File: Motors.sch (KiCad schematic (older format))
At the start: 11 parts

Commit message: Eletrical Rules Check
Fixed some label names
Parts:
- gave numbers to parts that had none: 11
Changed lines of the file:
@@
 i_mtr0
 $Comp
-L Connector:Conn_01x12_Female J?
+L Connector:Conn_01x12_Female J4
 U 1 1 5E6AD3E3
 P 8725 2125
-F 0 "J?" H 8753 2101 50  0000 L CNN
+F 0 "J4" H 8753 2101 50  0000 L CNN
 F 1 "Conn_01x12_Female" H 8753 2010 50  0000 L CNN
 F 2 "" H 8725 2125 50  0001 C CNN
@@
 	7975 2725 8525 2725
 $Comp
-L power:GND #PWR?
+L power:GND #PWR055
 U 1 1 5E6B1444
 P 7975 2125
-F 0 "#PWR?" H 7975 1875 50  0001 C CNN
+F 0 "#PWR055" H 7975 1875 50  0001 C CNN
 F 1 "GND" H 7980 1952 50  0000 C CNN
 F 2 "" H 7975 2125 50  0001 C CNN
@@
 $EndComp
 $Comp
-L power:GND #PWR?
+L power:GND #PWR056
 U 1 1 5E6B180E
 P 7975 2725
-F 0 "#PWR?" H 7975 2475 50  0001 C CNN
+F 0 "#PWR056" H 7975 2475 50  0001 C CNN
 F 1 "GND" H 7980 2552 50  0000 C CNN
 F 2 "" H 7975 2725 50  0001 C CNN
@@
 i_mtr1
 $Comp
-L Device:R R?
+L Device:R R20
 U 1 1 5E6FBB13
 P 6425 1250
-F 0 "R?" V 6218 1250 50  0000 C CNN
+F 0 "R20" V 6218 1250 50  0000 C CNN
 F 1 "R" V 6309 1250 50  0000 C CNN
 F 2 "" V 6355 1250 50  0001 C CNN
@@
 enc0_b
 $Comp
-L Device:R R?
+L Device:R R21
 U 1 1 5E700368
 P 6425 1550
-F 0 "R?" V 6218 1550 50  0000 C CNN
+F 0 "R21" V 6218 1550 50  0000 C CNN
 F 1 "R" V 6309 1550 50  0000 C CNN
 F 2 "" V 6355 1550 50  0001 C CNN
@@
 $EndComp
 $Comp
-L Device:R R?
+L Device:R R22
 U 1 1 5E701D8F
 P 6425 1850
-F 0 "R?" V 6218 1850 50  0000 C CNN
+F 0 "R22" V 6218 1850 50  0000 C CNN
 F 1 "R" V 6309 1850 50  0000 C CNN
 F 2 "" V 6355 1850 50  0001 C CNN
@@
 $EndComp
 $Comp
-L Device:R R?
+L Device:R R23
 U 1 1 5E7027C7
 P 6425 2150
-F 0 "R?" V 6218 2150 50  0000 C CNN
+F 0 "R23" V 6218 2150 50  0000 C CNN
 F 1 "R" V 6309 2150 50  0000 C CNN
 F 2 "" V 6355 2150 50  0001 C CNN
@@
 p_enc1
 $Comp
-L Device:Jumper JP?
+L Device:Jumper JP6
 U 1 1 5E67171D
 P 6500 2700
-F 0 "JP?" H 6500 2964 50  0000 C CNN
+F 0 "JP6" H 6500 2964 50  0000 C CNN
 F 1 "Jumper" H 6500 2873 50  0000 C CNN
 F 2 "" H 6500 2700 50  0001 C CNN
@@
 $EndComp
 $Comp
-L Device:Jumper JP?
+L Device:Jumper JP7
 U 1 1 5E673F70
 P 6500 3000
-F 0 "JP?" H 6500 3264 50  0000 C CNN
+F 0 "JP7" H 6500 3264 50  0000 C CNN
 F 1 "Jumper" H 6500 3173 50  0000 C CNN
 F 2 "" H 6500 3000 50  0001 C CNN
@@
 $EndComp
 $Comp
-L Device:Jumper JP?
+L Device:Jumper JP8
 U 1 1 5E6743E1
 P 6500 3300
-F 0 "JP?" H 6500 3564 50  0000 C CNN
+F 0 "JP8" H 6500 3564 50  0000 C CNN
 F 1 "Jumper" H 6500 3473 50  0000 C CNN
 F 2 "" H 6500 3300 50  0001 C CNN
@@
 $EndComp
 $Comp
-L Device:Jumper JP?
+L Device:Jumper JP9
 U 1 1 5E67477A
 P 6500 3600
-F 0 "JP?" H 6500 3864 50  0000 C CNN
+F 0 "JP9" H 6500 3864 50  0000 C CNN
 F 1 "Jumper" H 6500 3773 50  0000 C CNN
 F 2 "" H 6500 3600 50  0001 C CNN
@@
 $EndComp
 $Comp
-L Device:Jumper JP?
+L Device:Jumper JP10
 U 1 1 5E67668F
 P 6500 3900
-F 0 "JP?" H 6500 4164 50  0000 C CNN
+F 0 "JP10" H 6500 4164 50  0000 C CNN
 F 1 "Jumper" H 6500 4073 50  0000 C CNN
 F 2 "" H 6500 3900 50  0001 C CNN
@@
 $EndComp
 $Comp
-L Device:Jumper JP?
+L Device:Jumper JP11
 U 1 1 5E676935
 P 6500 4200
-F 0 "JP?" H 6500 4464 50  0000 C CNN
+F 0 "JP11" H 6500 4464 50  0000 C CNN
 F 1 "Jumper" H 6500 4373 50  0000 C CNN
 F 2 "" H 6500 4200 50  0001 C CNN
@@
 p_enc1
 $Comp
-L ec_2b_rescue:+3.3V #PWR?
+L ec_2b_rescue:+3.3V #PWR052
 U 1 1 5E67786E
 P 5700 2600
-F 0 "#PWR?" H 5700 2450 50  0001 C CNN
+F 0 "#PWR052" H 5700 2450 50  0001 C CNN
 F 1 "+3.3V" H 5715 2773 50  0000 C CNN
 F 2 "" H 5700 2600 50  0001 C CNN
@@
 $EndComp
 $Comp
-L ec_2b_rescue:+12V #PWR?
+L ec_2b_rescue:+12V #PWR054
 U 1 1 5E677F8F
 P 6100 2600
-F 0 "#PWR?" H 6100 2450 50  0001 C CNN
+F 0 "#PWR054" H 6100 2450 50  0001 C CNN
 F 1 "+12V" H 6115 2773 50  0000 C CNN
 F 2 "" H 6100 2600 50  0001 C CNN
@@
 $EndComp
 $Comp
-L ec_2b_rescue:+5V #PWR?
+L ec_2b_rescue:+5V #PWR053
 U 1 1 5E6785E6
 P 5900 2600
-F 0 "#PWR?" H 5900 2450 50  0001 C CNN
+F 0 "#PWR053" H 5900 2450 50  0001 C CNN
 F 1 "+5V" H 5915 2773 50  0000 C CNN
 F 2 "" H 5900 2600 50  0001 C CNN

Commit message: Formatting Changes
Made some minor formatting changes. Documented motor channels. Fixed in labels of motor channel.
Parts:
- removed J4: Conn_01x12_Female, symbol Connector:Conn_01x12_Female
- added J8, J9: Conn_01x06_Female, symbol Connector:Conn_01x06_Female
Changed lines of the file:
@@
 $Descr A4 11693 8268
 encoding utf-8
-Sheet 9 12
+Sheet 6 12
 Title ""
 Date ""
@@
 Text GLabel 3550 1900 0    50   Input ~ 0
 i_mtr0
-$Comp
-L Connector:Conn_01x12_Female J4
-U 1 1 5E6AD3E3
-P 8725 2125
-F 0 "J4" H 8753 2101 50  0000 L CNN
-F 1 "Conn_01x12_Female" H 8753 2010 50  0000 L CNN
-F 2 "" H 8725 2125 50  0001 C CNN
-F 3 "~" H 8725 2125 50  0001 C CNN
-	1    8725 2125
-	1    0    0    -1
-$EndComp
-Text Label 8525 1625 2    50   ~ 0
+Text Label 9525 1625 2    50   ~ 0
 mtr0_out1
-Text Label 8525 1725 2    50   ~ 0
+Text Label 9525 1725 2    50   ~ 0
 mtr0_out2
 Text GLabel 6575 1550 2    50   Input ~ 0
 enc0_a
-Text Label 8525 2225 2    50   ~ 0
+Text Label 9525 2325 2    50   ~ 0
 mtr1_out1
-Text Label 8525 2325 2    50   ~ 0
+Text Label 9525 2425 2    50   ~ 0
 mtr1_out2
 Text GLabel 6575 2150 2    50   Input ~ 0
@@
 enc1_b
 Wire Wire Line
-	7975 2025 8525 2025
-Wire Wire Line
-	7975 2125 8525 2125
-Wire Wire Line
-	7975 2625 8525 2625
-Wire Wire Line
-	7975 2725 8525 2725
+	8975 2025 9525 2025
+Wire Wire Line
+	8975 2125 9525 2125
+Wire Wire Line
+	8975 2725 9525 2725
+Wire Wire Line
+	8975 2825 9525 2825
 $Comp
 L power:GND #PWR055
 U 1 1 5E6B1444
-P 7975 2125
-F 0 "#PWR055" H 7975 1875 50  0001 C CNN
-F 1 "GND" H 7980 1952 50  0000 C CNN
-F 2 "" H 7975 2125 50  0001 C CNN
-F 3 "" H 7975 2125 50  0001 C CNN
-	1    7975 2125
+P 8975 2125
+F 0 "#PWR055" H 8975 1875 50  0001 C CNN
+F 1 "GND" H 8980 1952 50  0000 C CNN
+F 2 "" H 8975 2125 50  0001 C CNN
+F 3 "" H 8975 2125 50  0001 C CNN
+	1    8975 2125
 	1    0    0    -1
 $EndComp
@@
 L power:GND #PWR056
 U 1 1 5E6B180E
-P 7975 2725
-F 0 "#PWR056" H 7975 2475 50  0001 C CNN
-F 1 "GND" H 7980 2552 50  0000 C CNN
-F 2 "" H 7975 2725 50  0001 C CNN
-F 3 "" H 7975 2725 50  0001 C CNN
-	1    7975 2725
-	1    0    0    -1
-$EndComp
-Text Label 8025 2725 0    50   ~ 0
+P 8975 2825
+F 0 "#PWR056" H 8975 2575 50  0001 C CNN
+F 1 "GND" H 8980 2652 50  0000 C CNN
+F 2 "" H 8975 2825 50  0001 C CNN
+F 3 "" H 8975 2825 50  0001 C CNN
+	1    8975 2825
+	1    0    0    -1
+$EndComp
+Text Label 9025 2825 0    50   ~ 0
 mtr_encoder
-Text Label 8025 2125 0    50   ~ 0
+Text Label 9025 2125 0    50   ~ 0
 mtr_encoder
 Text GLabel 6575 1250 2    50   Input ~ 0
@@
 Text GLabel 3550 2800 0    50   Input ~ 0
 i_mtr1
-$Comp
-L Device:R R20
-U 1 1 5E6FBB13
-P 6425 1250
-F 0 "R20" V 6218 1250 50  0000 C CNN
-F 1 "R" V 6309 1250 50  0000 C CNN
-F 2 "" V 6355 1250 50  0001 C CNN
-F 3 "~" H 6425 1250 50  0001 C CNN
-	1    6425 1250
-	0    1    1    0
-$EndComp
-Text Label 8525 1825 2    50   ~ 0
+Text Label 9525 1825 2    50   ~ 0
 enc0_a
-Text Label 8525 1925 2    50   ~ 0
+Text Label 9525 1925 2    50   ~ 0
 enc0_b
-Text Label 8525 2425 2    50   ~ 0
+Text Label 9525 2525 2    50   ~ 0
 enc1_a
-Text Label 8525 2525 2    50   ~ 0
+Text Label 9525 2625 2    50   ~ 0
 enc1_b
 Text Label 6275 1250 2    50   ~ 0
@@
 U 1 1 5E700368
 P 6425 1550
-F 0 "R21" V 6218 1550 50  0000 C CNN
-F 1 "R" V 6309 1550 50  0000 C CNN
+F 0 "R21" V 6325 1550 50  0000 C CNN
+F 1 "R" V 6425 1550 50  0000 C CNN
 F 2 "" V 6355 1550 50  0001 C CNN
 F 3 "~" H 6425 1550 50  0001 C CNN
@@
 U 1 1 5E701D8F
 P 6425 1850
-F 0 "R22" V 6218 1850 50  0000 C CNN
-F 1 "R" V 6309 1850 50  0000 C CNN
+F 0 "R22" V 6325 1850 50  0000 C CNN
+F 1 "R" V 6425 1850 50  0000 C CNN
 F 2 "" V 6355 1850 50  0001 C CNN
 F 3 "~" H 6425 1850 50  0001 C CNN
 	1    6425 1850
-	0    1    1    0
-$EndComp
-$Comp
-L Device:R R23
-U 1 1 5E7027C7
-P 6425 2150
-F 0 "R23" V 6218 2150 50  0000 C CNN
-F 1 "R" V 6309 2150 50  0000 C CNN
-F 2 "" V 6355 2150 50  0001 C CNN
-F 3 "~" H 6425 2150 50  0001 C CNN
-	1    6425 2150
 	0    1    1    0
 $EndComp
@@
 Text GLabel 4750 2800 2    50   Input ~ 0
 mtr1_pwm
-Text Label 7975 2025 0    50   ~ 0
+Text Label 8975 2025 0    50   ~ 0
 p_enc0
-Text Label 7975 2625 0    50   ~ 0
+Text Label 8975 2725 0    50   ~ 0
 p_enc1
 $Comp
@@
 Wire Wire Line
 	6100 3300 6100 4200
+$Comp
+L Connector:Conn_01x06_Female J8
+U 1 1 5E6B3280
+P 9725 1825
+F 0 "J8" H 9753 1801 50  0000 L CNN
+F 1 "Conn_01x06_Female" H 9753 1710 50  0000 L CNN
+F 2 "" H 9725 1825 50  0001 C CNN
+F 3 "~" H 9725 1825 50  0001 C CNN
+	1    9725 1825
+	1    0    0    -1
+$EndComp
+$Comp
+L Connector:Conn_01x06_Female J9
+U 1 1 5E6B4D9E
+P 9725 2525
+F 0 "J9" H 9753 2501 50  0000 L CNN
+F 1 "Conn_01x06_Female" H 9753 2410 50  0000 L CNN
+F 2 "" H 9725 2525 50  0001 C CNN
+F 3 "~" H 9725 2525 50  0001 C CNN
+	1    9725 2525
+	1    0    0    -1
+$EndComp
+$Comp
+L Device:R R20
+U 1 1 5E6FBB13
+P 6425 1250
+F 0 "R20" V 6325 1250 50  0000 C CNN
+F 1 "R" V 6400 1250 50  0000 C TNN
+F 2 "" V 6355 1250 50  0001 C CNN
+F 3 "~" H 6425 1250 50  0001 C CNN
+	1    6425 1250
+	0    1    1    0
+$EndComp
+$Comp
+L Device:R R23
+U 1 1 5E750250
+P 6425 2150
+F 0 "R23" V 6325 2150 50  0000 C CNN
+F 1 "R" V 6425 2150 50  0000 C CNN
+F 2 "" V 6355 2150 50  0001 C CNN
+F 3 "~" H 6425 2150 50  0001 C CNN
+	1    6425 2150
+	0    1    1    0
+$EndComp
 $EndSCHEMATC

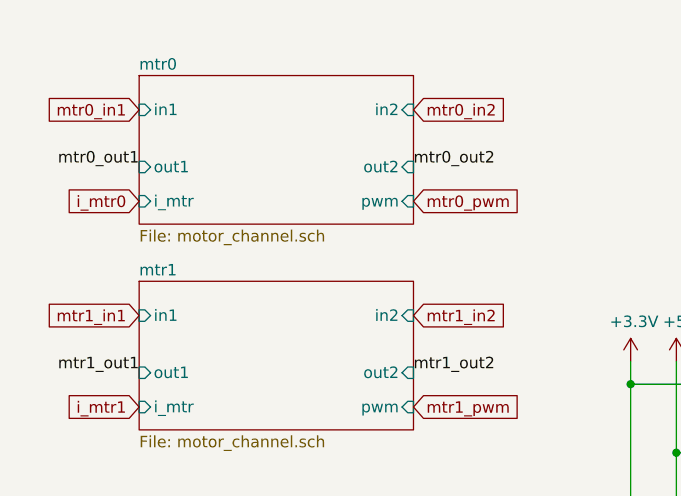
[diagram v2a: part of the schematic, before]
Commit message: renamed motor controller input name and moved adc pinouts
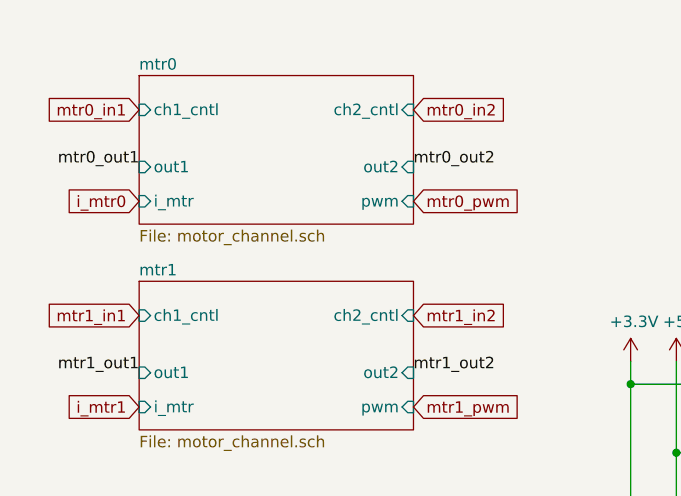
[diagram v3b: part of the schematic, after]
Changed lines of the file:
@@
 F0 "mtr0" 50
 F1 "motor_channel.sch" 50
-F2 "in1" I L 3550 1500 50
-F3 "in2" I R 4750 1500 50
+F2 "ch1_cntl" I L 3550 1500 50
+F3 "ch2_cntl" I R 4750 1500 50
 F4 "i_mtr" I L 3550 1900 50
 F5 "out1" I L 3550 1750 50
@@
 F0 "mtr1" 50
 F1 "motor_channel.sch" 50
-F2 "in1" I L 3550 2400 50
-F3 "in2" I R 4750 2400 50
+F2 "ch1_cntl" I L 3550 2400 50
+F3 "ch2_cntl" I R 4750 2400 50
 F4 "i_mtr" I L 3550 2800 50
 F5 "out1" I L 3550 2650 50

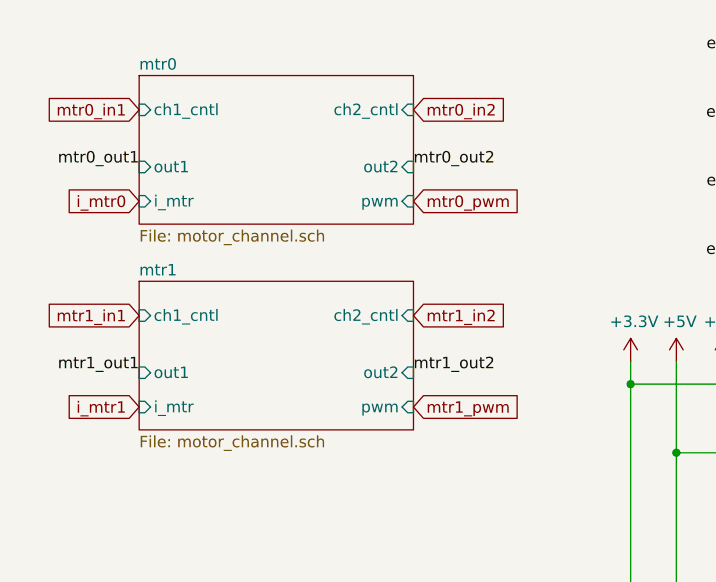
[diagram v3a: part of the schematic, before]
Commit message: fixed up pwm control to hbridge
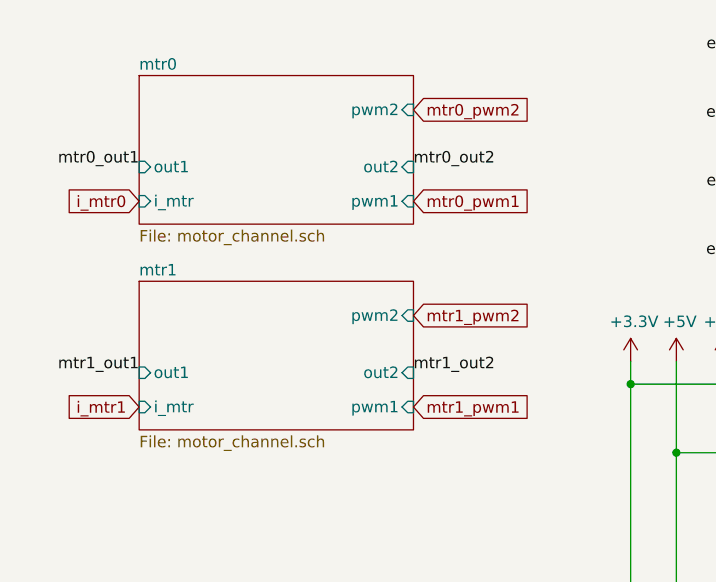
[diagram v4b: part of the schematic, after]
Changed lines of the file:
@@
 F0 "mtr0" 50
 F1 "motor_channel.sch" 50
-F2 "ch1_cntl" I L 3550 1500 50
-F3 "ch2_cntl" I R 4750 1500 50
-F4 "i_mtr" I L 3550 1900 50
-F5 "out1" I L 3550 1750 50
-F6 "out2" I R 4750 1750 50
-F7 "pwm" I R 4750 1900 50
+F2 "i_mtr" I L 3550 1900 50
+F3 "out1" I L 3550 1750 50
+F4 "out2" I R 4750 1750 50
+F5 "pwm1" I R 4750 1900 50
+F6 "pwm2" I R 4750 1500 50
 $EndSheet
 Text Label 3550 1750 2    50   ~ 0
@@
 Text Label 4750 1750 0    50   ~ 0
 mtr0_out2
-Text GLabel 3550 1500 0    50   Input ~ 0
-mtr0_in1
 Text GLabel 4750 1500 2    50   Input ~ 0
-mtr0_in2
+mtr0_pwm2
 Text GLabel 3550 1900 0    50   Input ~ 0
 i_mtr0
@@
 F0 "mtr1" 50
 F1 "motor_channel.sch" 50
-F2 "ch1_cntl" I L 3550 2400 50
-F3 "ch2_cntl" I R 4750 2400 50
-F4 "i_mtr" I L 3550 2800 50
-F5 "out1" I L 3550 2650 50
-F6 "out2" I R 4750 2650 50
-F7 "pwm" I R 4750 2800 50
+F2 "pwm2" I R 4750 2400 50
+F3 "i_mtr" I L 3550 2800 50
+F4 "out1" I L 3550 2650 50
+F5 "out2" I R 4750 2650 50
+F6 "pwm1" I R 4750 2800 50
 $EndSheet
 Text Label 3550 2650 2    50   ~ 0
@@
 Text Label 4750 2650 0    50   ~ 0
 mtr1_out2
-Text GLabel 3550 2400 0    50   Input ~ 0
-mtr1_in1
 Text GLabel 4750 2400 2    50   Input ~ 0
-mtr1_in2
+mtr1_pwm2
 Text GLabel 3550 2800 0    50   Input ~ 0
 i_mtr1
@@
 enc1_b
 Text GLabel 4750 1900 2    50   Input ~ 0
-mtr0_pwm
+mtr0_pwm1
 Text GLabel 4750 2800 2    50   Input ~ 0
-mtr1_pwm
+mtr1_pwm1
 Text Label 8975 2025 0    50   ~ 0
 p_enc0

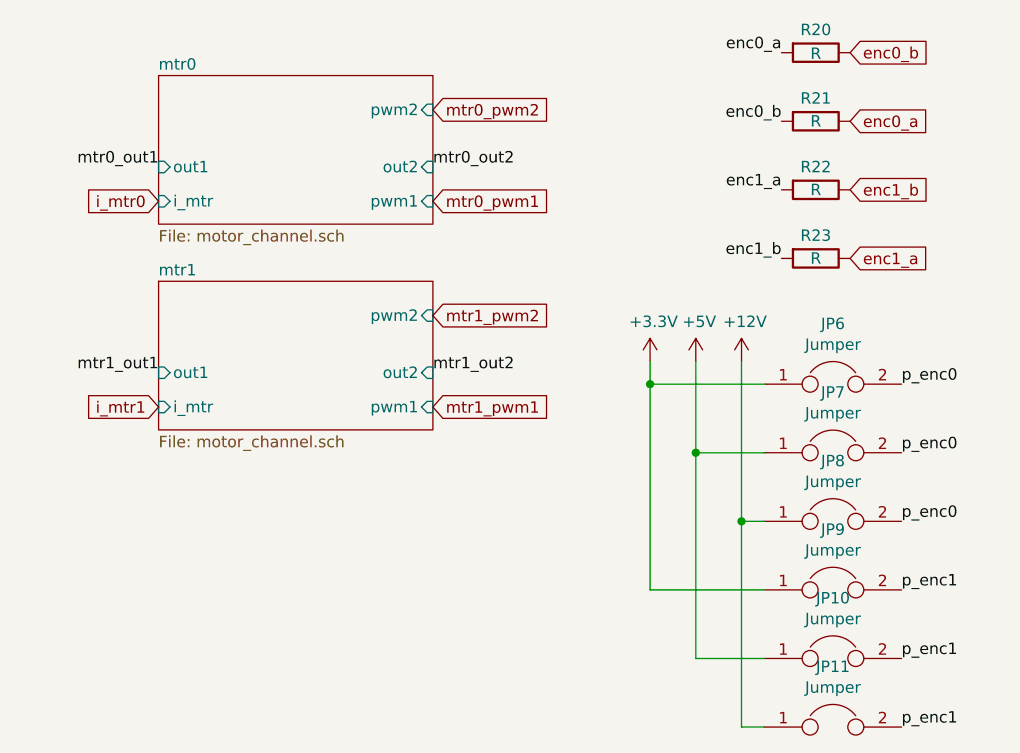
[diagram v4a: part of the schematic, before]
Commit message: Motor Channel Cleanup
Removed some leftover labels in the motor channel after removal of the AND gate. Renumbering.
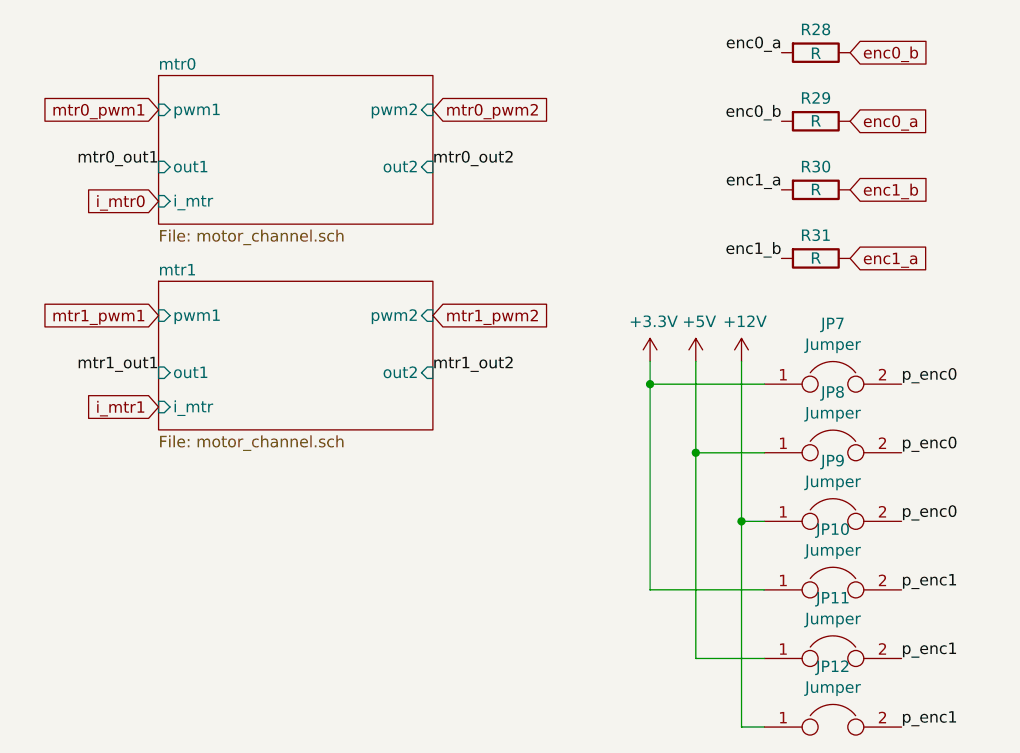
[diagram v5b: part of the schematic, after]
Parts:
- renumbered JP9 to JP10, JP10 to JP11, JP11 to JP12, JP6 to JP7, JP7 to JP8, JP8 to JP9, R20 to R28, R21 to R29, R22 to R30, R23 to R31
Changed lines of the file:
@@
 $Descr A4 11693 8268
 encoding utf-8
-Sheet 6 12
+Sheet 10 12
 Title ""
 Date ""
@@
 F3 "out1" I L 3550 1750 50
 F4 "out2" I R 4750 1750 50
-F5 "pwm1" I R 4750 1900 50
+F5 "pwm1" I L 3550 1500 50
 F6 "pwm2" I R 4750 1500 50
 $EndSheet
@@
 	8975 2825 9525 2825
 $Comp
-L power:GND #PWR055
+L power:GND #PWR089
 U 1 1 5E6B1444
 P 8975 2125
-F 0 "#PWR055" H 8975 1875 50  0001 C CNN
+F 0 "#PWR089" H 8975 1875 50  0001 C CNN
 F 1 "GND" H 8980 1952 50  0000 C CNN
 F 2 "" H 8975 2125 50  0001 C CNN
@@
 $EndComp
 $Comp
-L power:GND #PWR056
+L power:GND #PWR090
 U 1 1 5E6B180E
 P 8975 2825
-F 0 "#PWR056" H 8975 2575 50  0001 C CNN
+F 0 "#PWR090" H 8975 2575 50  0001 C CNN
 F 1 "GND" H 8980 2652 50  0000 C CNN
 F 2 "" H 8975 2825 50  0001 C CNN
@@
 F4 "out1" I L 3550 2650 50
 F5 "out2" I R 4750 2650 50
-F6 "pwm1" I R 4750 2800 50
+F6 "pwm1" I L 3550 2400 50
 $EndSheet
 Text Label 3550 2650 2    50   ~ 0
@@
 enc0_b
 $Comp
-L Device:R R21
+L Device:R R29
 U 1 1 5E700368
 P 6425 1550
-F 0 "R21" V 6325 1550 50  0000 C CNN
+F 0 "R29" V 6325 1550 50  0000 C CNN
 F 1 "R" V 6425 1550 50  0000 C CNN
 F 2 "" V 6355 1550 50  0001 C CNN
@@
 $EndComp
 $Comp
-L Device:R R22
+L Device:R R30
 U 1 1 5E701D8F
 P 6425 1850
-F 0 "R22" V 6325 1850 50  0000 C CNN
+F 0 "R30" V 6325 1850 50  0000 C CNN
 F 1 "R" V 6425 1850 50  0000 C CNN
 F 2 "" V 6355 1850 50  0001 C CNN
@@
 Text Label 6275 2150 2    50   ~ 0
 enc1_b
-Text GLabel 4750 1900 2    50   Input ~ 0
+Text GLabel 3550 1500 0    50   Input ~ 0
 mtr0_pwm1
-Text GLabel 4750 2800 2    50   Input ~ 0
+Text GLabel 3550 2400 0    50   Input ~ 0
 mtr1_pwm1
 Text Label 8975 2025 0    50   ~ 0
@@
 p_enc1
 $Comp
-L Device:Jumper JP6
+L Device:Jumper JP7
 U 1 1 5E67171D
 P 6500 2700
-F 0 "JP6" H 6500 2964 50  0000 C CNN
+F 0 "JP7" H 6500 2964 50  0000 C CNN
 F 1 "Jumper" H 6500 2873 50  0000 C CNN
 F 2 "" H 6500 2700 50  0001 C CNN
@@
 $EndComp
 $Comp
-L Device:Jumper JP7
+L Device:Jumper JP8
 U 1 1 5E673F70
 P 6500 3000
-F 0 "JP7" H 6500 3264 50  0000 C CNN
+F 0 "JP8" H 6500 3264 50  0000 C CNN
 F 1 "Jumper" H 6500 3173 50  0000 C CNN
 F 2 "" H 6500 3000 50  0001 C CNN
@@
 $EndComp
 $Comp
-L Device:Jumper JP8
+L Device:Jumper JP9
 U 1 1 5E6743E1
 P 6500 3300
-F 0 "JP8" H 6500 3564 50  0000 C CNN
+F 0 "JP9" H 6500 3564 50  0000 C CNN
 F 1 "Jumper" H 6500 3473 50  0000 C CNN
 F 2 "" H 6500 3300 50  0001 C CNN
@@
 $EndComp
 $Comp
-L Device:Jumper JP9
+L Device:Jumper JP10
 U 1 1 5E67477A
 P 6500 3600
-F 0 "JP9" H 6500 3864 50  0000 C CNN
+F 0 "JP10" H 6500 3864 50  0000 C CNN
 F 1 "Jumper" H 6500 3773 50  0000 C CNN
 F 2 "" H 6500 3600 50  0001 C CNN
@@
 $EndComp
 $Comp
-L Device:Jumper JP10
+L Device:Jumper JP11
 U 1 1 5E67668F
 P 6500 3900
-F 0 "JP10" H 6500 4164 50  0000 C CNN
+F 0 "JP11" H 6500 4164 50  0000 C CNN
 F 1 "Jumper" H 6500 4073 50  0000 C CNN
 F 2 "" H 6500 3900 50  0001 C CNN
@@
 $EndComp
 $Comp
-L Device:Jumper JP11
+L Device:Jumper JP12
 U 1 1 5E676935
 P 6500 4200
-F 0 "JP11" H 6500 4464 50  0000 C CNN
+F 0 "JP12" H 6500 4464 50  0000 C CNN
 F 1 "Jumper" H 6500 4373 50  0000 C CNN
 F 2 "" H 6500 4200 50  0001 C CNN
@@
 p_enc1
 $Comp
-L ec_2b_rescue:+3.3V #PWR052
+L ec_2b_rescue:+3.3V #PWR086
 U 1 1 5E67786E
 P 5700 2600
-F 0 "#PWR052" H 5700 2450 50  0001 C CNN
+F 0 "#PWR086" H 5700 2450 50  0001 C CNN
 F 1 "+3.3V" H 5715 2773 50  0000 C CNN
 F 2 "" H 5700 2600 50  0001 C CNN
@@
 $EndComp
 $Comp
-L ec_2b_rescue:+12V #PWR054
+L ec_2b_rescue:+12V #PWR088
 U 1 1 5E677F8F
 P 6100 2600
-F 0 "#PWR054" H 6100 2450 50  0001 C CNN
+F 0 "#PWR088" H 6100 2450 50  0001 C CNN
 F 1 "+12V" H 6115 2773 50  0000 C CNN
 F 2 "" H 6100 2600 50  0001 C CNN
@@
 $EndComp
 $Comp
-L ec_2b_rescue:+5V #PWR053
+L ec_2b_rescue:+5V #PWR087
 U 1 1 5E6785E6
 P 5900 2600
-F 0 "#PWR053" H 5900 2450 50  0001 C CNN
+F 0 "#PWR087" H 5900 2450 50  0001 C CNN
 F 1 "+5V" H 5915 2773 50  0000 C CNN
 F 2 "" H 5900 2600 50  0001 C CNN
@@
 $EndComp
 $Comp
-L Device:R R20
+L Device:R R28
 U 1 1 5E6FBB13
 P 6425 1250
-F 0 "R20" V 6325 1250 50  0000 C CNN
+F 0 "R28" V 6325 1250 50  0000 C CNN
 F 1 "R" V 6400 1250 50  0000 C TNN
 F 2 "" V 6355 1250 50  0001 C CNN
@@
 $EndComp
 $Comp
-L Device:R R23
+L Device:R R31
 U 1 1 5E750250
 P 6425 2150
-F 0 "R23" V 6325 2150 50  0000 C CNN
+F 0 "R31" V 6325 2150 50  0000 C CNN
 F 1 "R" V 6425 2150 50  0000 C CNN
 F 2 "" V 6355 2150 50  0001 C CNN
